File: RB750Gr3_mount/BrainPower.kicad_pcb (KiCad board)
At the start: 2 copper layers, 149.9 x 111.3 mm, 9 parts, among them J1 BarrelJack_CUI_PJ-063AH_Horiz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, P1 Golden finger, PCIeX1, Dual, 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

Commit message: add optional soldering pads for 12V
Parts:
- added J2: PhoenixContact_MCV_1,5_2-G-5.08_1x02_P5.08mm_Vertical, Connector_Phoenix_MC_HighVoltage:PhoenixContact_MCV_1,5_2-G-5.08_1x02_P5.08mm_Vertical, F.Cu at (212.7, 111.1)
- J1: value BarrelJack_CUI_PJ-063AH_Horizontal -> BarrelJack_Horizontal; footprint Connector_BarrelJack:BarrelJack_CUI_PJ-063AH_Horizontal -> Connector_BarrelJack:BarrelJack_Horizontal
- moved J1 0.17 mm to (215.3, 139.7), turned to 270 degrees
- renumbered MH3 to MH2
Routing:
- net +12V: track 109.1 -> 138.7 mm
- net GND: track 102.7 -> 131.4 mm
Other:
- board text added: "- + DC 12V Center+"
- board text removed: "DC 12V Center+"

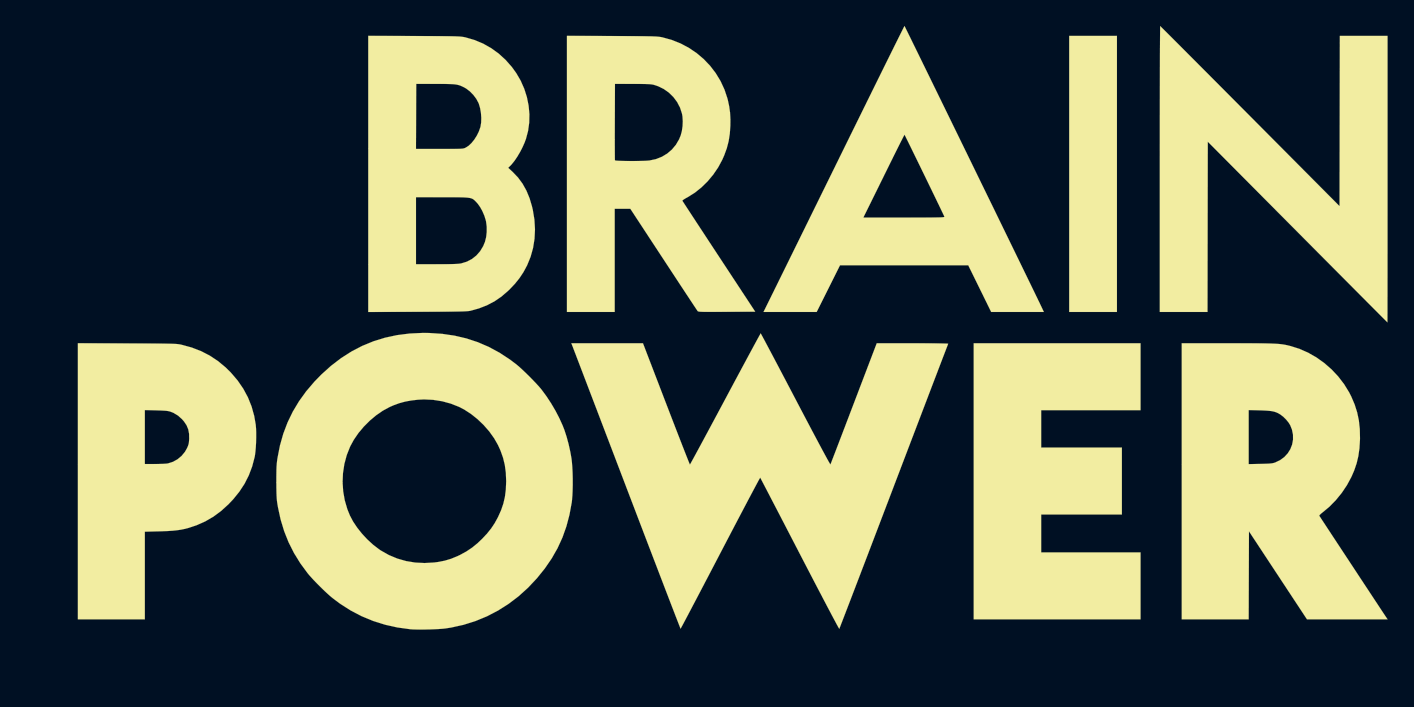
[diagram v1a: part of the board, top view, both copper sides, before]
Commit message: remove unused footprints
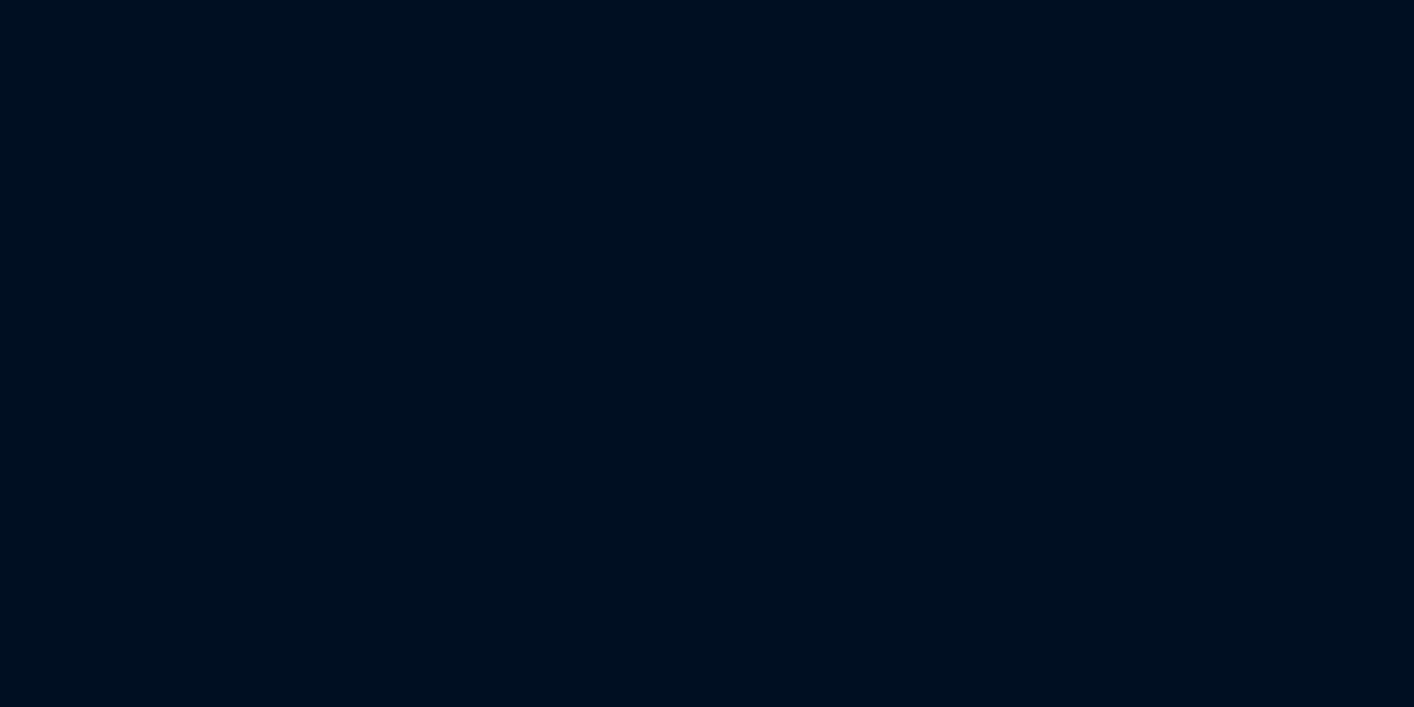
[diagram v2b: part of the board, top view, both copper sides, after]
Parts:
- removed the Ref** at (221.0, -163.8)

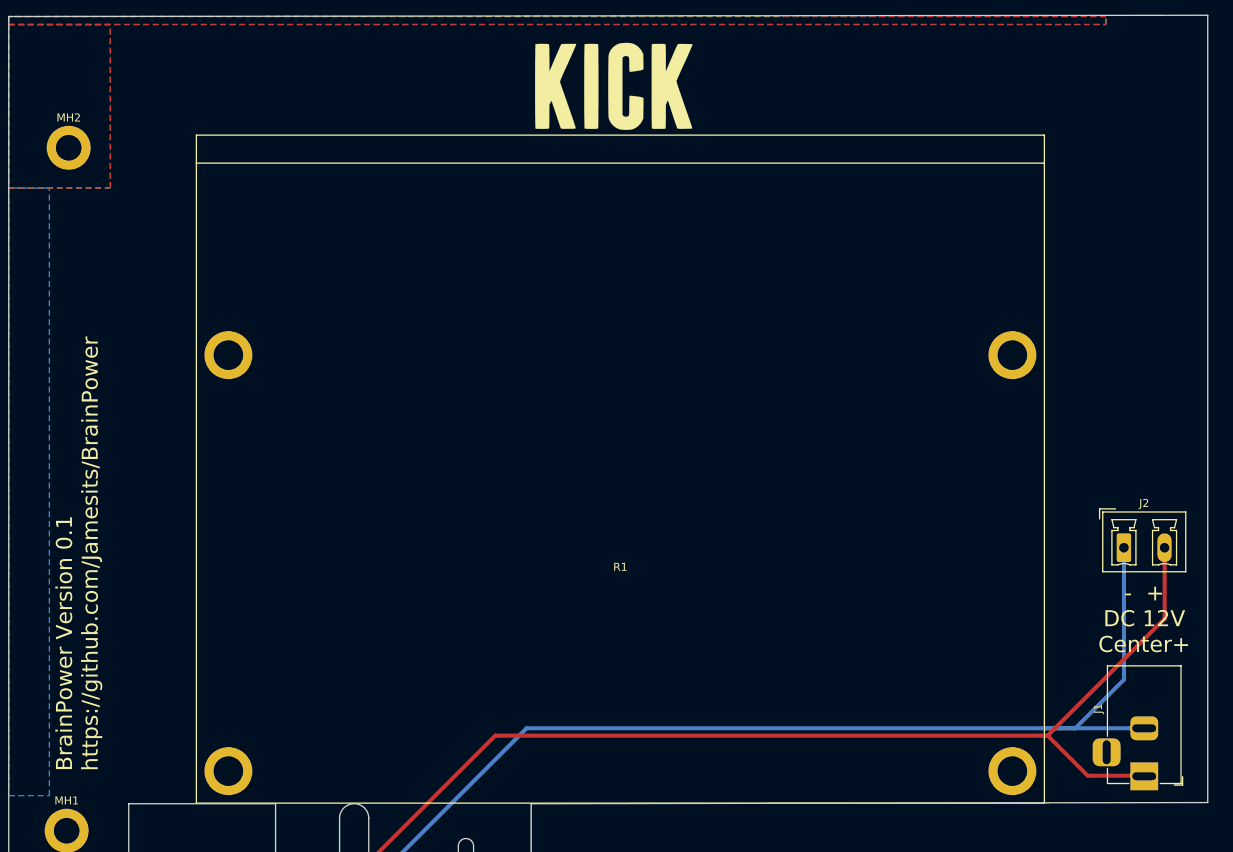
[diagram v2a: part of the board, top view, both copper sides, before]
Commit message: added compatibility for RB450 series
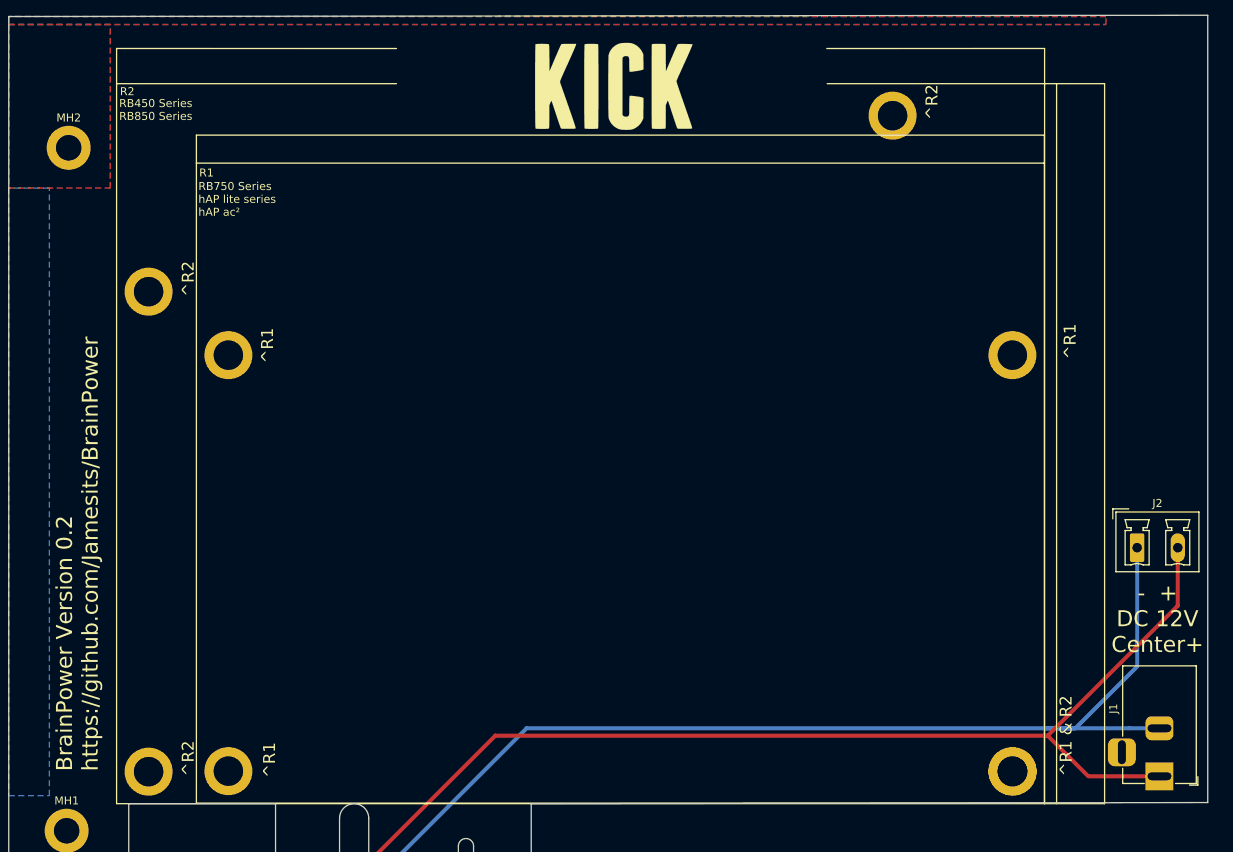
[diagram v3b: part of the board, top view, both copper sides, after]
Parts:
- added R2: RB450Gx4, Footprints:RB450Gx4, F.Cu at (147.2, 101.4)
- moved J1 1.91 mm to (217.2, 139.7)
- moved J2 1.65 mm to (214.4, 111.1)
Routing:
- net GND: track 131.4 -> 134.0 mm
- net +12V: track 138.7 -> 141.2 mm
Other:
- board text added: "0.2"
- board text added: "Brain Power RB750/RB450 PCI express Mounting Plate"
- board text added: "BrainPower Version 0.2 https://github.com/Jamesits/BrainPower"
- board text added: "RB450 Series RB850 Series"
- board text added: "RB750 Series hAP lite series hAP ac²"
- board text added: "^R1"
- board text added: "^R1 & R2"
- board text added: "^R2"
- board text removed: "0.1"
- board text removed: "Brain Power RB750Gr3 Mounting Plate"
- board text removed: "BrainPower Version 0.1 https://github.com/Jamesits/BrainPower"
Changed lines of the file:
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@@
   (general
     (thickness 1.6)
-    (drawings 27)
+    (drawings 36)
     (tracks 16)
     (zones 0)
-    (modules 9)
+    (modules 10)
     (nets 3)
   )
@@
     (diff_pair_gap 0.25)
   )
+  (module Footprints:RB450Gx4 (layer F.Cu)
+    (at 147.18538 101.3714)
+    (fp_text reference R2 (at -59.04738 -47.2694 180) (layer F.SilkS)
+      (effects (font (size 1 1) (thickness 0.15)))
+    )
+    (fp_text value RB450Gx4 (at -0.0635 0.8048 180) (layer F.Fab)
+      (effects (font (size 1 1) (thickness 0.15)))
+    )
+    (fp_text user LED (at 59.9313 -11.049 -90) (layer Dwgs.User)
+      (effects (font (size 1 1) (thickness 0.15)))
+    )
+    (fp_text user "DC Jack" (at 59.9313 13.0175 -90) (layer Dwgs.User)
+      (effects (font (size 1 1) (thickness 0.15)))
+    )
+    (fp_text user "Serial Port" (at 60.0456 -37.1094 -90) (layer Dwgs.User)
+      (effects (font (size 1 1) (thickness 0.15)))
+    )
+    (fp_text user "RJ45 Ports" (at -0.0762 -50.4317 180) (layer Dwgs.User)
+      (effects (font (size 1 1) (thickness 0.15)))
+    )
+    (fp_line (start 57.1242 41.7527) (end 57.1242 -48.2473) (layer F.SilkS) (width 0.12))
+    (fp_line (start 63.1242 -48.2473) (end 55.6242 -48.2473) (layer F.SilkS) (width 0.12))
+    (fp_line (start 63.1242 41.7527) (end 63.1242 -48.2473) (layer F.SilkS) (width 0.12))
+    (fp_line (start 55.6242 41.7527) (end 63.1242 41.7527) (layer F.SilkS) (width 0.12))
+    (fp_line (start 55.6242 -52.6473) (end 55.6242 -48.2473) (layer F.SilkS) (width 0.12))
+    (fp_line (start 28.3972 -52.6415) (end 55.6242 -52.6473) (layer F.SilkS) (width 0.12))
+    (fp_line (start -60.3758 -48.2473) (end -60.3758 -52.6473) (layer F.SilkS) (width 0.12))
+    (fp_line (start 55.6242 -48.2473) (end 28.448 -48.2473) (layer F.SilkS) (width 0.12))
+    (fp_line (start 55.6242 41.7527) (end 55.6242 -48.2473) (layer F.SilkS) (width 0.12))
+    (fp_line (start -60.3758 41.7527) (end 55.6242 41.7527) (layer F.SilkS) (width 0.12))
+    (fp_line (start -60.3758 -48.2473) (end -60.3758 41.7527) (layer F.SilkS) (width 0.12))
+    (fp_line (start -60.3758 -52.6473) (end -25.3873 -52.6415) (layer F.SilkS) (width 0.12))
+    (fp_line (start -25.3873 -48.2473) (end -60.3758 -48.2473) (layer F.SilkS) (width 0.12))
+    (pad 3 thru_hole circle (at -56.3758 37.7527 180) (size 6 6) (drill 3.7) (layers *.Cu *.Mask))
+    (pad 4 thru_hole circle (at 51.6242 37.7527 180) (size 6 6) (drill 3.7) (layers *.Cu *.Mask))
+    (pad 1 thru_hole circle (at -56.3758 -22.2473 180) (size 6 6) (drill 3.7) (layers *.Cu *.Mask))
+    (pad 2 thru_hole circle (at 36.6242 -44.2473 180) (size 6 6) (drill 3.7) (layers *.Cu *.Mask))
+  )
   (module Connector_Phoenix_MC_HighVoltage:PhoenixContact_MCV_1,5_2-G-5.08_1x02_P5.08mm_Vertical (layer F.Cu)
-    (at 212.725 111.125)
+    (at 214.376 111.125)
     (descr "Generic Phoenix Contact connector footprint for: MCV_1,5/2-G-5.08; number of pins: 02; pin pitch: 5.08mm; Vertical || order number: 1836299 8A 320V")
     (tags "phoenix_contact connector MCV_01x02_G_5.08mm")
@@
     (pad 2 thru_hole oval (at 5.08 0) (size 1.8 3.6) (drill 1.2) (layers *.Cu *.Mask)
       (net 2 +12V))
-    (pad 1 thru_hole roundrect (at 0 0) (size 1.8 3.6) (drill 1.2) (layers *.Cu *.Mask) (roundrect_rratio 0.139)
+    (pad 1 thru_hole roundrect (at 0 0) (size 1.8 3.6) (drill 1.2) (layers *.Cu *.Mask) (roundrect_rratio 0.138889)
       (net 1 GND))
     (model ${KISYS3DMOD}/Connector_Phoenix_MC_HighVoltage.3dshapes/PhoenixContact_MCV_1,5_2-G-5.08_1x02_P5.08mm_Vertical.wrl
@@
   )
   (module Connector_BarrelJack:BarrelJack_Horizontal (layer F.Cu)
-    (at 215.265 139.7 270)
+    (at 217.17 139.7 270)
     (descr "DC Barrel Jack")
     (tags "Power Jack")
@@
   (module Footprints:RB750Gr3 (layer F.Cu)
     (at 149.7838 113.0554)
-    (fp_text reference R1 (at 0 0.5) (layer F.SilkS)
+    (fp_text reference R1 (at -51.7398 -48.7934) (layer F.SilkS)
       (effects (font (size 1 1) (thickness 0.15)))
     )
     (fp_text value RB750Gr3 (at 0 -0.5) (layer F.Fab)
+      (effects (font (size 1 1) (thickness 0.15)))
+    )
+    (fp_text user "RJ45 Ports" (at 0.2032 -51.6509) (layer Dwgs.User)
       (effects (font (size 1 1) (thickness 0.15)))
     )
@@
     (pad A17 smd rect (at 8.5 0) (size 0.7 4.2) (layers B.Cu B.Paste B.Mask))
   )
-  (gr_text "BrainPower Version 0.1\nhttps://github.com/Jamesits/BrainPower" (at 81.915 139.065 90) (layer F.SilkS)
+  (gr_text ^R1 (at 205.994 85.344 90) (layer F.SilkS)
+    (effects (font (size 1.5 1.5) (thickness 0.15)))
+  )
+  (gr_text ^R1 (at 105.918 137.668 90) (layer F.SilkS)
+    (effects (font (size 1.5 1.5) (thickness 0.15)))
+  )
+  (gr_text ^R1 (at 105.664 85.852 90) (layer F.SilkS)
+    (effects (font (size 1.5 1.5) (thickness 0.15)))
+  )
+  (gr_text "^R1 & R2" (at 205.486 139.7 90) (layer F.SilkS)
+    (effects (font (size 1.5 1.5) (thickness 0.15)) (justify left))
+  )
+  (gr_text ^R2 (at 188.722 57.658 90) (layer F.SilkS)
+    (effects (font (size 1.5 1.5) (thickness 0.15)) (justify left))
+  )
+  (gr_text ^R2 (at 95.758 139.7 90) (layer F.SilkS)
+    (effects (font (size 1.5 1.5) (thickness 0.15)) (justify left))
+  )
+  (gr_text ^R2 (at 95.758 79.756 90) (layer F.SilkS)
+    (effects (font (size 1.5 1.5) (thickness 0.15)) (justify left))
+  )
+  (gr_text "RB450 Series\nRB850 Series" (at 87.122 56.388) (layer F.SilkS)
+    (effects (font (size 1 1) (thickness 0.15)) (justify left))
+  )
+  (gr_text "RB750 Series\nhAP lite series\nhAP ac²" (at 97.028 67.564) (layer F.SilkS)
+    (effects (font (size 1 1) (thickness 0.15)) (justify left))
+  )
+  (gr_text "BrainPower Version 0.2\nhttps://github.com/Jamesits/BrainPower" (at 81.915 139.065 90) (layer F.SilkS)
     (effects (font (size 2 2) (thickness 0.25)) (justify left))
   )
-  (gr_text "-  +\nDC 12V\nCenter+" (at 215.265 120.015) (layer F.SilkS)
+  (gr_text "-  +\nDC 12V\nCenter+" (at 216.916 120.015) (layer F.SilkS)
     (effects (font (size 2 2) (thickness 0.3)))
   )
@@
     (effects (font (size 2 2) (thickness 0.15)))
   )
-  (gr_text 0.1 (at 268.4272 193.0908) (layer Cmts.User)
+  (gr_text 0.2 (at 268.4272 193.0908) (layer Cmts.User)
     (effects (font (size 2 2) (thickness 0.15)) (justify left))
   )
-  (gr_text "Brain Power RB750Gr3 Mounting Plate" (at 186.4868 189.3316) (layer Cmts.User)
+  (gr_text "Brain Power RB750/RB450 PCI express Mounting Plate" (at 186.4868 189.3316) (layer Cmts.User)
     (effects (font (size 2 2) (thickness 0.15)) (justify left))
   )
@@
   (gr_arc (start 116.505 144.9546) (end 118.33 144.9546) (angle -180) (layer Edge.Cuts) (width 0.1))
   (gr_line (start 118.33 155.3796) (end 118.33 144.9546) (layer Edge.Cuts) (width 0.1))
-  (segment (start 213.415 133.7) (end 215.265 133.7) (width 0.5) (layer B.Cu) (net 1))
   (segment (start 121.98 149.7796) (end 138.0596 133.7) (width 0.5) (layer B.Cu) (net 1))
   (segment (start 121.98 152.3796) (end 121.98 149.7796) (width 0.5) (layer B.Cu) (net 1))
-  (segment (start 202.85 133.7) (end 206.66 133.7) (width 0.5) (layer B.Cu) (net 1))
   (segment (start 138.0596 133.7) (end 202.85 133.7) (width 0.5) (layer B.Cu) (net 1))
   (segment (start 202.85 133.7) (end 213.415 133.7) (width 0.5) (layer B.Cu) (net 1))
-  (segment (start 212.725 127.635) (end 212.725 111.125) (width 0.5) (layer B.Cu) (net 1))
-  (segment (start 206.66 133.7) (end 212.725 127.635) (width 0.5) (layer B.Cu) (net 1))
+  (segment (start 214.376 125.984) (end 214.376 111.125) (width 0.5) (layer B.Cu) (net 1))
+  (segment (start 202.85 133.7) (end 206.66 133.7) (width 0.5) (layer B.Cu) (net 1))
+  (segment (start 206.66 133.7) (end 214.376 125.984) (width 0.5) (layer B.Cu) (net 1))
+  (segment (start 213.415 133.7) (end 217.17 133.7) (width 0.5) (layer B.Cu) (net 1))
   (segment (start 118.98 150.6296) (end 118.98 152.3796) (width 0.254) (layer F.Cu) (net 2))
   (segment (start 118.98 149.7796) (end 134.1396 134.62) (width 0.5) (layer F.Cu) (net 2))
   (segment (start 118.98 152.3796) (end 118.98 149.7796) (width 0.5) (layer F.Cu) (net 2))
   (segment (start 134.1396 134.62) (end 203.2 134.62) (width 0.5) (layer F.Cu) (net 2))
-  (segment (start 208.2038 139.6238) (end 215.4174 139.6238) (width 0.5) (layer F.Cu) (net 2))
-  (segment (start 203.2 134.62) (end 208.2038 139.6238) (width 0.5) (layer F.Cu) (net 2))
-  (segment (start 203.2 134.62) (end 217.805 120.015) (width 0.5) (layer F.Cu) (net 2))
-  (segment (start 217.805 120.015) (end 217.805 111.125) (width 0.5) (layer F.Cu) (net 2))
+  (segment (start 208.28 139.7) (end 217.17 139.7) (width 0.5) (layer F.Cu) (net 2))
+  (segment (start 203.2 134.62) (end 208.28 139.7) (width 0.5) (layer F.Cu) (net 2))
+  (segment (start 219.456 118.364) (end 219.456 111.125) (width 0.5) (layer F.Cu) (net 2))
+  (segment (start 203.2 134.62) (end 219.456 118.364) (width 0.5) (layer F.Cu) (net 2))
   (zone (net 0) (net_name "") (layer B.Mask) (hatch edge 0.508)
     (connect_pads (clearance 0.508))
